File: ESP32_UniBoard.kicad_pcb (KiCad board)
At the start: 4 copper layers, 34 x 52.3 mm, 30 parts, among them J1 USB_C_Receptacle_USB2.0, J2 Conn_01x06_Socket, J3 Hirose DF40C, SW1 SW_Push, SW2 SW_Push, U1 ESP32-S3-WROOM-1, U2 AZ1117-3.3, U3 USBLC6-2SC6

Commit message: Additional routing~
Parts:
- moved C5 0.22 mm to (136.2, 90.7)
- moved SW2 0.22 mm to (131.8, 93.3)
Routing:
- net (no net): track 0.00 -> 83.1 mm
- net /GPIO16: track 0.00 -> 39.5 mm, vias 0 -> 1
- net /GPIO17: track 0.00 -> 35.9 mm, vias 0 -> 1
- net /GPIO18: track 0.00 -> 32.4 mm, vias 0 -> 1
- net /GPIO8: track 0.00 -> 26.3 mm, vias 0 -> 1
- net /GPIO36: track 0.00 -> 25.2 mm, vias 0 -> 1
- net /GPIO35: track 0.00 -> 23.5 mm, vias 0 -> 1
- net /BOOT: track 1.97 -> 22.7 mm, vias 0 -> 1
- net /GPIO3: track 0.00 -> 18.9 mm, vias 0 -> 1
- net /GPIO45: track 0.00 -> 18.9 mm, vias 0 -> 1
- net /GPIO48: track 0.00 -> 18.5 mm, vias 0 -> 1
- net /GPIO46: track 0.00 -> 18.5 mm, vias 0 -> 1
- net /GPIO47: track 0.00 -> 18.3 mm, vias 0 -> 1
- net /GPIO9: track 0.00 -> 18.3 mm, vias 0 -> 1
- net /GPIO21: track 0.00 -> 17.9 mm, vias 0 -> 1
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
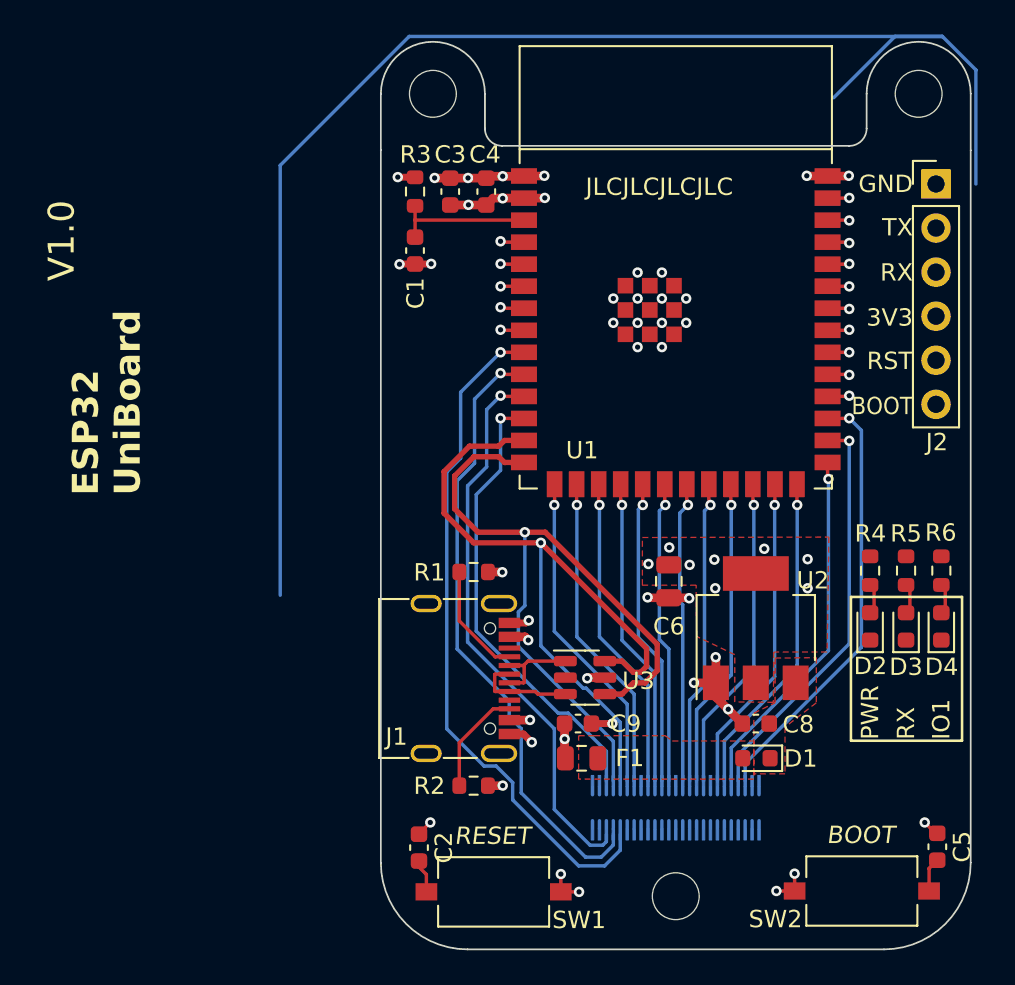
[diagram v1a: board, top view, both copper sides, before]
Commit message: Routing 4 Layer Board complete
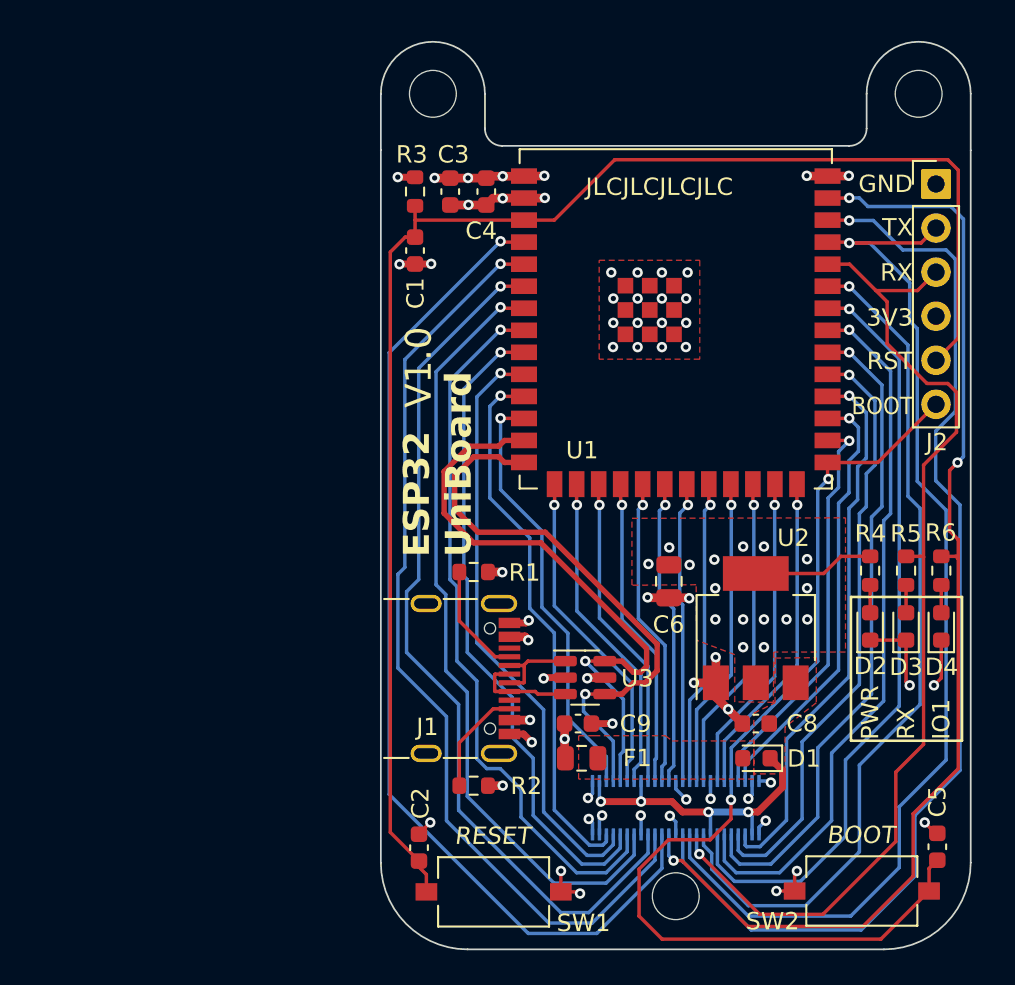
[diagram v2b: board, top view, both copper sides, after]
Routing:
- net (no net): track 83.1 -> 0.00 mm
- net /EN: track 10.0 -> 85.8 mm
- net /GPIO1: track 1.25 -> 67.1 mm, vias 1 -> 3
- net /GPIO2: track 1.26 -> 63.9 mm
- net /ESP_TX: track 1.27 -> 62.7 mm
- net /ESP_RX: track 1.26 -> 59.9 mm
- net /GPIO4: track 1.37 -> 58.5 mm
- net /GPIO5: track 1.36 -> 54.5 mm
- net /GPIO6: track 1.35 -> 50.9 mm
- net /GPIO42: track 1.25 -> 49.9 mm
- net /GPIO7: track 1.37 -> 45.4 mm
- net /GPIO41: track 1.27 -> 44.7 mm
- net /GPIO15: track 1.36 -> 41.8 mm
- net /GPIO40: track 1.26 -> 41.2 mm
- net /BOOT: track 22.7 -> 60.1 mm, vias 1 -> 2
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- added copper zone on F.Cu, net GND

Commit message: Slight changes and added JLCPCB part numbers
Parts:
- D1: value D_Schottky -> B5819W SL; footprint Diode_SMD:D_0603_1608Metric -> Diode_SMD:D_SOD-123
- D3: value RED -> YL
- F1: value Polyfuse -> 1.1 A
- J3: value Hirose DF40C -> dHirose DF40C-50DS
- R4: value R -> 680R
- R5, R6: value R -> 1k8
- moved D1 0.92 mm to (124.8, 85.7)
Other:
- rule pad_to_mask_clearance: 0 -> 0.04
- board text added: "V1.1"
- board text removed: "V1.0"
